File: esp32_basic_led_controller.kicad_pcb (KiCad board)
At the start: 2 copper layers, 16 parts, among them J1 Barrel_Jack_Switch_Pin3Ring, J2 Conn_01x03, J3 Screw_Terminal_01x02, Q1 IRF8721PBF-1, SW1 SW_DIP_x01, U1 ESP32-WROOM-32U, U2 LD1117S33TR_SOT223, U3 I2C_SENS_1

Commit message: PCB layout
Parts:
- moved J3 35.5 mm to (179.4, 94.1)
- moved Q1 24.4 mm to (169.3, 105.7), turned to 90 degrees
- moved R3 19.8 mm to (167.9, 98.9), turned to -90 degrees
- moved J1 18.3 mm to (122.6, 103.5)
- moved C1 12.7 mm to (122.1, 90.0), turned to 90 degrees
- moved C2 11.3 mm to (128.2, 88.5), turned to 180 degrees
- moved R5 8.82 mm to (167.9, 95.1), turned to -90 degrees
- moved R1 6.99 mm to (140.0, 112.4), turned to -90 degrees
- moved SW1 6.98 mm to (131.6, 112.3)
- moved R2 6.52 mm to (147.7, 110.4)
- moved D1 6.00 mm to (153.1, 110.5), turned to 180 degrees
- moved U2 4.64 mm to (130.2, 95.5)
- moved U3 4.54 mm to (162.9, 90.7)
- moved J2 3.66 mm to (163.9, 103.0)
- moved R4 3.65 mm to (167.9, 91.3), turned to -90 degrees
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
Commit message: Updated PCB layout
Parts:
- added REF**: MountingHole_2.2mm_M2_DIN965_Pad, MountingHole:MountingHole_2.2mm_M2_DIN965_Pad, F.Cu at (177.8, 85.3)
- added REF**: MountingHole_2.2mm_M2_DIN965_Pad, MountingHole:MountingHole_2.2mm_M2_DIN965_Pad, F.Cu at (177.8, 116.8)
- added REF**: MountingHole_2.2mm_M2_DIN965_Pad, MountingHole:MountingHole_2.2mm_M2_DIN965_Pad, F.Cu at (116.8, 116.8)
- added REF**: MountingHole_2.2mm_M2_DIN965_Pad, MountingHole:MountingHole_2.2mm_M2_DIN965_Pad, F.Cu at (116.8, 85.3)
- moved R1 13.5 mm to (127.6, 107.0)
- moved R3 12.8 mm to (169.2, 111.6), turned to 0 degrees
- moved U3 6.54 mm to (167.5, 95.3), turned to -90 degrees
- moved J3 6.22 mm to (179.4, 100.3), turned to 90 degrees
- moved C1 5.51 mm to (122.8, 95.5), turned to 180 degrees
- moved R4 5.14 mm to (162.8, 90.9), turned to 180 degrees
- moved R5 4.22 mm to (168.4, 90.9), turned to 180 degrees
- moved C2 1.86 mm to (130.0, 88.5)
- moved Q1 0.17 mm to (169.2, 105.7)
- turned SW1 to 180 degrees
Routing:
- net +12V: track 0.00 -> 94.9 mm
- net +3.3V: track 0.00 -> 75.9 mm, vias 0 -> 2
- net GPIO0: track 0.00 -> 38.7 mm
- net TX0: track 0.00 -> 27.4 mm, vias 0 -> 1
- net GPIO19: track 0.00 -> 24.2 mm, vias 0 -> 2
- net RX0: track 0.00 -> 23.7 mm, vias 0 -> 1
- net Net-(J3-Pin_2): track 0.00 -> 21.3 mm
- net Net-(U1-IO16): track 0.00 -> 18.9 mm, vias 0 -> 2
- net GPIO18: track 0.00 -> 14.2 mm
- net Net-(Q1-G): track 0.00 -> 3.91 mm
- net Net-(D1-A): track 0.00 -> 3.01 mm
- added copper zone on B.Cu, net GND
- added copper zone on F.Cu, net GND
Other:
- board outline added: 69.6 x 39.6 mm
- board text added: "+12V"
- board text added: "3.3V"
- board text added: "ESP32 LED Light Controller"
- board text added: "GND"
- board text added: "RX"
- board text added: "Rev. 1.0 © 2023 https://iosnerd.com"
- board text added: "SCL"
- board text added: "SDA"
- board text added: "TX"

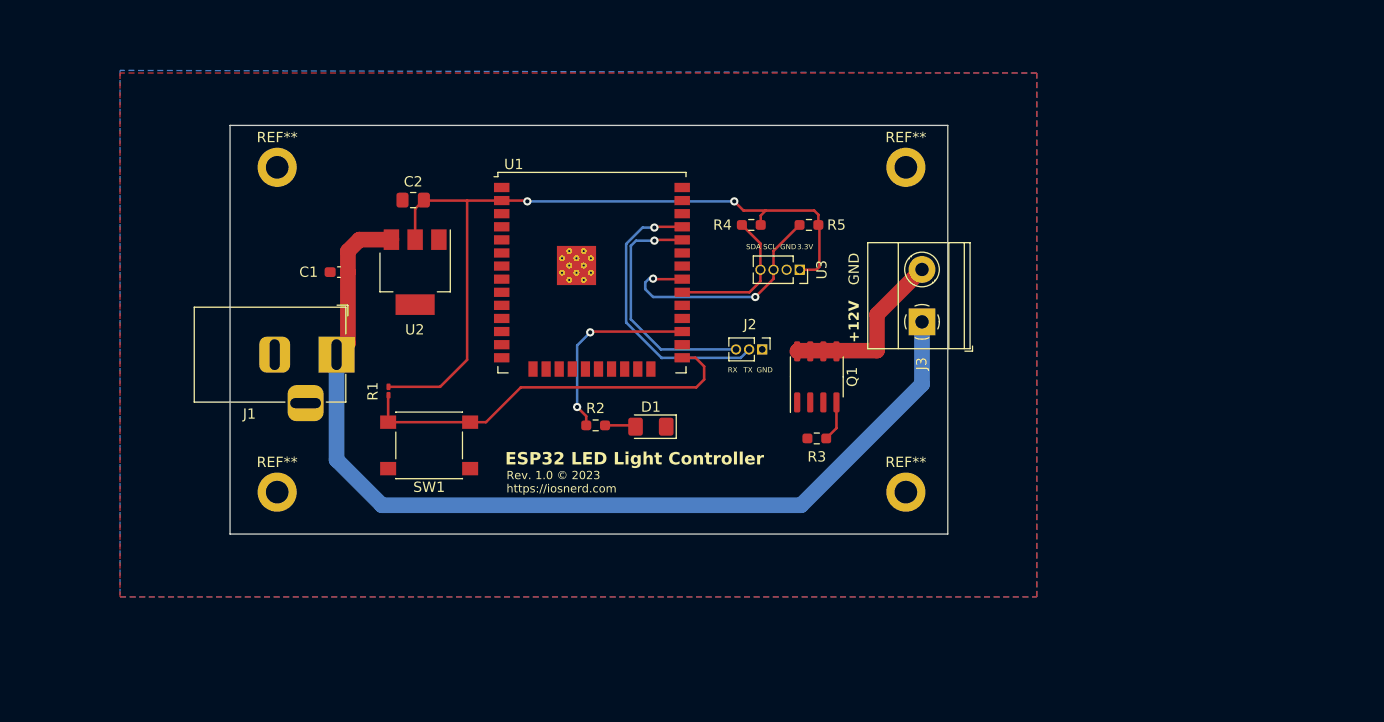
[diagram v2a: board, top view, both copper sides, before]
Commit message: Vertical board layout
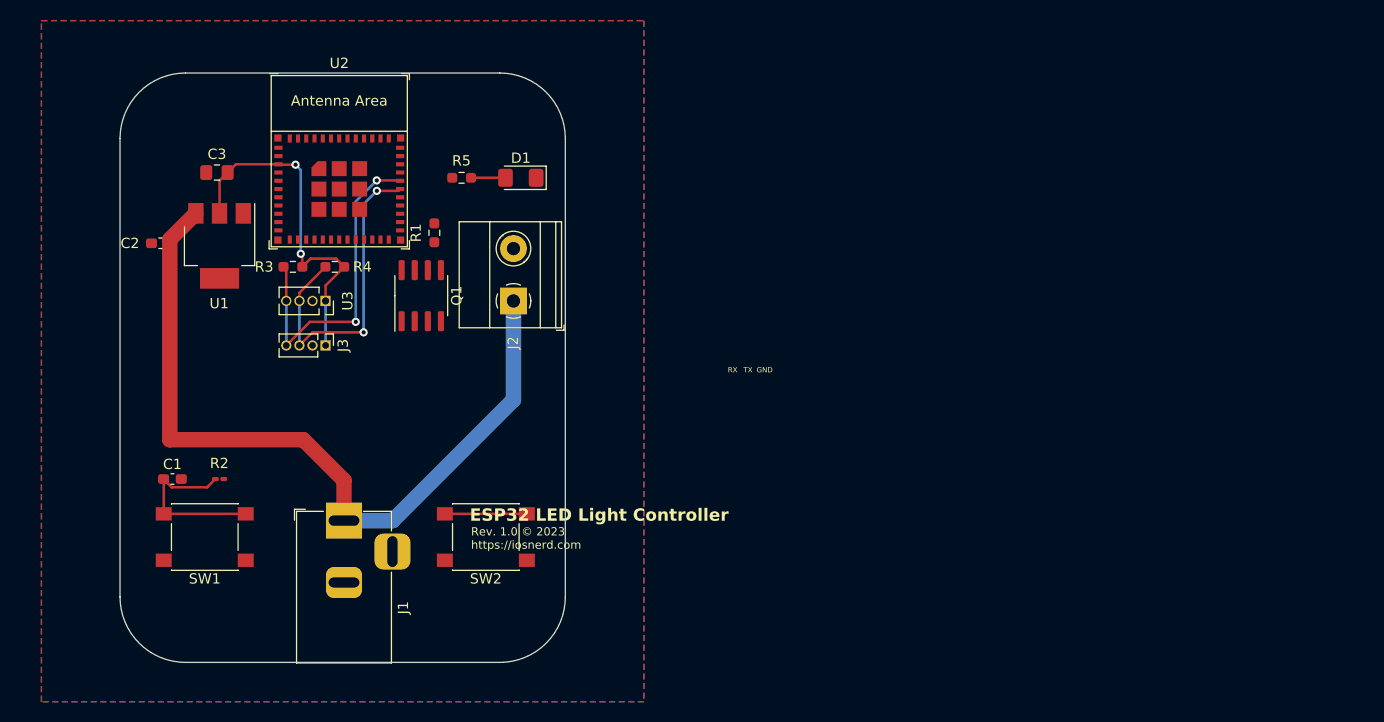
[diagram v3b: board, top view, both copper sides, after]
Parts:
- removed REF** (x4): MountingHole_2.2mm_M2_DIN965_Pad, MountingHole:MountingHole_2.2mm_M2_DIN965_Pad
- removed the U1 at (147.4, 95.6)
- added C1: 1μF, Capacitor_SMD:C_0603_1608Metric_Pad1.08x0.95mm_HandSolder, F.Cu at (106.7, 115.6)
- added SW2: SW_DIP_x01, Button_Switch_SMD:SW_Push_1P1T_NO_6x6mm_H9.5mm, F.Cu at (137.1, 121.2)
- added U2: ESP32-C3-MINI-1, PCM_Espressif:ESP32-C3-MINI-1, F.Cu at (122.9, 84.8)
- J3: renamed from J2; value Conn_01x03 -> Conn_01x04; footprint Connector_PinHeader_1.27mm:PinHeader_1x03_P1.27mm_Vertical -> Connector_PinHeader_1.27mm:PinHeader_1x04_P1.27mm_Vertical
- R1: renamed from R3; value 220R -> 220K
- R2: renamed from R1; value 2K -> 5.1K
- R5: renamed from R2; value 68R -> 5.1K
- moved R4 46.2 mm to (122.4, 95.0)
- moved U3 46.1 mm to (121.5, 98.3)
- moved R3 44.6 mm to (118.4, 95.0)
- moved J3 42.3 mm to (121.5, 102.6)
- moved R1 42.1 mm to (132.1, 91.7), turned to -90 degrees
- moved J2 39.7 mm to (139.8, 98.3)
- moved Q1 39.2 mm to (130.8, 97.8)
- moved R5 27.3 mm to (134.7, 86.4)
- moved D1 27.2 mm to (140.5, 86.4)
- moved SW1 23.5 mm to (109.8, 121.2)
- moved C3 19.2 mm to (111.0, 85.9)
- moved U1 19.1 mm to (111.3, 93.0)
- moved R2 18.5 mm to (111.3, 115.6), turned to 180 degrees
- moved C2 17.5 mm to (105.5, 92.7)
- moved J1 16.1 mm to (123.3, 119.6), turned to 90 degrees
- renumbered C1 to C2, C2 to C3, J3 to J2, R4 to R3, R5 to R4, U2 to U1
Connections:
- net GPIO0 renamed /RESET
- J3 pad 1: GND -> +3.3V
- J3 pad 2: TX0 -> GND
- J3 pad 3: RX0 -> /RX
- R1 pad 1: GPIO25 -> /GPIO8
- R3 pad 2: GPIO18 -> /TX
- R4 pad 2: GPIO19 -> /RX
- R5 pad 1: Net-(U1-IO16) -> /GPIO2
- U3 pad 3: GPIO19 -> /RX
- U3 pad 4: GPIO18 -> /TX
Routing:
- net +3.3V: track 75.9 -> 34.5 mm
- net /TX: track 0.00 -> 32.3 mm, vias 0 -> 2
- net /RX: track 0.00 -> 32.0 mm, vias 0 -> 2
- net TX0: track 27.4 -> 0.00 mm, vias 1 -> 0
- net GPIO19: track 24.2 -> 0.00 mm, vias 2 -> 0
- net RX0: track 23.7 -> 0.00 mm, vias 1 -> 0
- net /RESET: track 38.7 -> 17.0 mm
- net Net-(J2-Pin_2): track 21.3 -> 0.00 mm
- net Net-(U1-IO16): track 18.9 -> 0.00 mm, vias 2 -> 0
- net +12V: track 94.9 -> 76.3 mm
- net GPIO18: track 14.2 -> 0.00 mm
- net /GPIO9: track 0.00 -> 7.95 mm
- net Net-(Q1-G): track 3.91 -> 0.00 mm
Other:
- board size 69.6 x 39.6 mm -> 43.2 x 57.1 mm
- board text removed: "+12V"
- board text removed: "3.3V"
- board text removed: "SCL"
- board text removed: "SDA"

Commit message: Board layout tweaks
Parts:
- added H1: MountingHole, MountingHole:MountingHole_2.2mm_M2_DIN965, F.Cu at (106.7, 80.0)
- added H2: MountingHole, MountingHole:MountingHole_2.2mm_M2_DIN965, F.Cu at (139.7, 80.0)
- added H3: MountingHole, MountingHole:MountingHole_2.2mm_M2_DIN965, F.Cu at (106.7, 116.8)
- added H4: MountingHole, MountingHole:MountingHole_2.2mm_M2_DIN965, F.Cu at (139.7, 116.8)
- D1: footprint LED_SMD:LED_1206_3216Metric_Pad1.42x1.75mm_HandSolder -> LED_SMD:LED_0603_1608Metric_Pad1.05x0.95mm_HandSolder
- R2: footprint Resistor_SMD:R_0201_0603Metric_Pad0.64x0.40mm_HandSolder -> Resistor_SMD:R_0603_1608Metric_Pad0.98x0.95mm_HandSolder
- moved D1 19.2 mm to (123.6, 95.5)
- moved R5 17.4 mm to (119.9, 95.5)
- moved J1 13.4 mm to (123.3, 106.2)
- moved R2 12.4 mm to (105.4, 104.6), turned to -90 degrees
- moved C1 11.0 mm to (108.2, 104.6), turned to 90 degrees
- moved SW2 11.0 mm to (137.9, 110.2)
- moved SW1 11.0 mm to (109.5, 110.2)
- moved R1 8.49 mm to (138.7, 97.0), turned to 0 degrees
- moved Q1 7.05 mm to (137.0, 101.2), turned to 180 degrees
- moved R3 6.73 mm to (117.1, 101.6), turned to -90 degrees
- moved R4 6.14 mm to (117.1, 98.0), turned to -90 degrees
- moved J2 5.84 mm to (139.8, 92.5)
- moved J3 5.08 mm to (124.2, 98.3), turned to 0 degrees
- moved C3 1.98 mm to (112.5, 87.1)
- moved U3 1.14 mm to (120.4, 98.3), turned to 0 degrees
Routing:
- net +3.3V: track 34.5 -> 57.4 mm
- net +12V: track 76.3 -> 54.5 mm
- net Net-(J2-Pin_2): track 0.00 -> 21.7 mm
- net /GPIO9: track 7.95 -> 26.5 mm
- net /GPIO8: track 0.00 -> 14.9 mm, vias 0 -> 2
- net /GPIO2: track 0.00 -> 10.7 mm, vias 0 -> 2
- net /RX: track 32.0 -> 25.7 mm, vias 2 -> 1
- net /TX: track 32.3 -> 27.8 mm, vias 2 -> 1
- net /RESET: track 17.0 -> 14.1 mm
- net Net-(Q1-G): track 0.00 -> 2.35 mm
- net Net-(D1-A): track 3.34 -> 1.91 mm
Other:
- board size 43.2 x 57.1 mm -> 43.2 x 44.2 mm

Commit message: Finished PCB routing and layout
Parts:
- SW1, SW2: value SW_DIP_x01 -> TSA343G00-250J2; footprint Button_Switch_SMD:SW_Push_1P1T_NO_6x6mm_H9.5mm -> User:TSA343G00-250J2
- moved SW2 24.8 mm to (136.2, 85.5), turned to -90 degrees
- moved C3 24.1 mm to (117.0, 110.8), turned to -90 degrees
- moved R2 19.5 mm to (113.8, 87.0)
- moved J2 17.9 mm to (139.5, 110.3)
- moved C2 17.3 mm to (117.0, 105.6), turned to 90 degrees
- moved U1 15.9 mm to (109.7, 108.8), turned to 180 degrees
- moved C1 15.1 mm to (113.8, 90.6)
- moved R1 10.4 mm to (128.4, 98.8), turned to -90 degrees
- moved SW1 9.18 mm to (110.8, 101.2), turned to 90 degrees
- moved Q1 4.05 mm to (134.8, 97.8), turned to 0 degrees
- moved D1 2.47 mm to (121.1, 95.3), turned to -90 degrees
- moved R5 0.63 mm to (119.3, 95.3), turned to -90 degrees
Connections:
- R5 pad 1: /GPIO2 -> /GPIO1
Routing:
- net +12V: track 54.5 -> 28.5 mm
- net /GPIO9: track 26.5 -> 13.5 mm
- net Net-(J2-Pin_2): track 21.7 -> 10.3 mm
- net /GPIO2: track 10.7 -> 0.00 mm, vias 2 -> 0
- net /GPIO8: track 14.9 -> 6.51 mm, vias 2 -> 0
- net +3.3V: track 57.4 -> 50.4 mm, vias 2 -> 4
- net /RESET: track 14.1 -> 17.2 mm
- net /GPIO1: track 0.00 -> 2.19 mm
- net Net-(Q1-G): track 2.35 -> 3.93 mm
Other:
- board size 43.2 x 44.2 mm -> 43.2 x 44.3 mm
- rule pad_to_mask_clearance: 0 -> 0.0508
- board text added: "+12V"
- board text added: "3.3V"
- board text added: "BOOT"
- board text added: "DC IN 12V"
- board text added: "ESP32 Light Controller"
- board text added: "RESET"
- board text added: "SCL"
- board text added: "SDA"
- board text removed: "ESP32 LED Light Controller"
- board text removed: "RX"
- board text removed: "TX"
